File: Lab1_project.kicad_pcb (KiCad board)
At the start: 2 copper layers, 80 x 80 mm, 11 parts, among them J1 PROG, J2 POWER IN, U1 STM32F407IGTx, U2 AMS1117-3.3, Y1 8 MHz

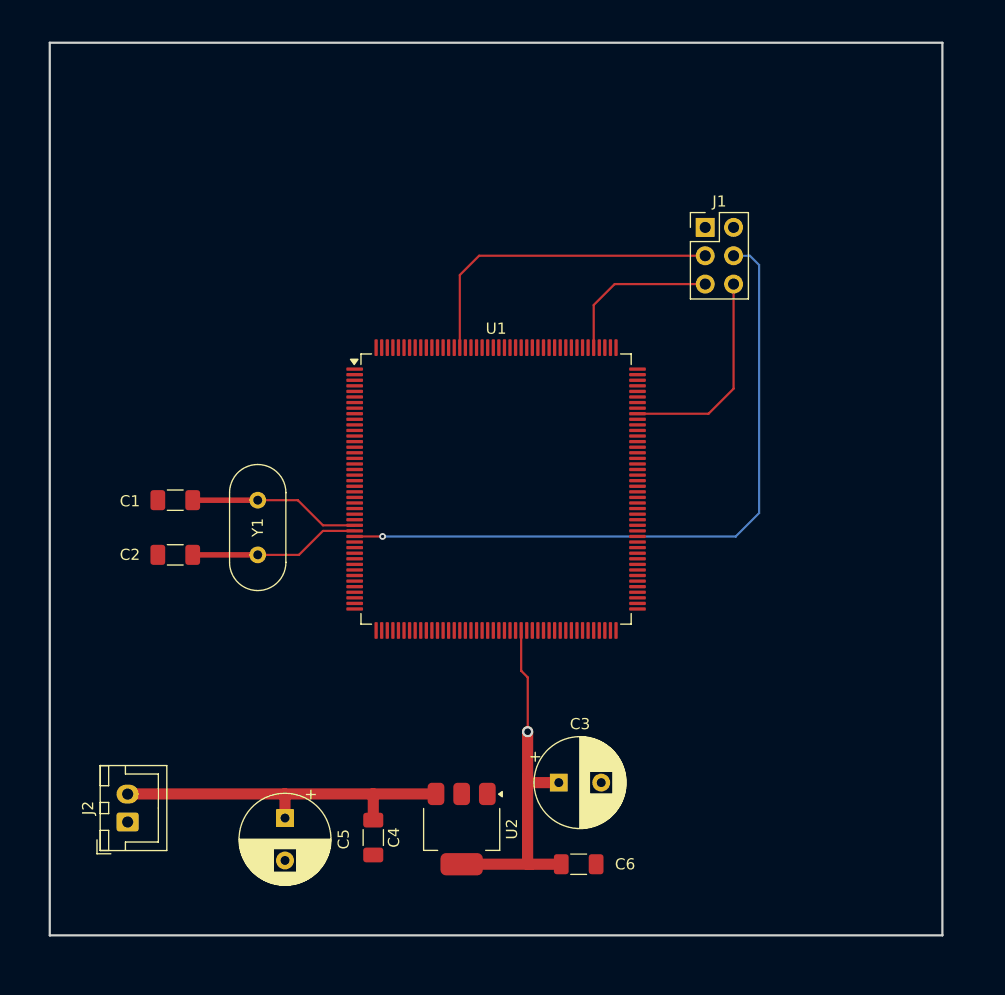
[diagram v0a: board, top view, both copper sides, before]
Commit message: fix: GND area, silkscreen
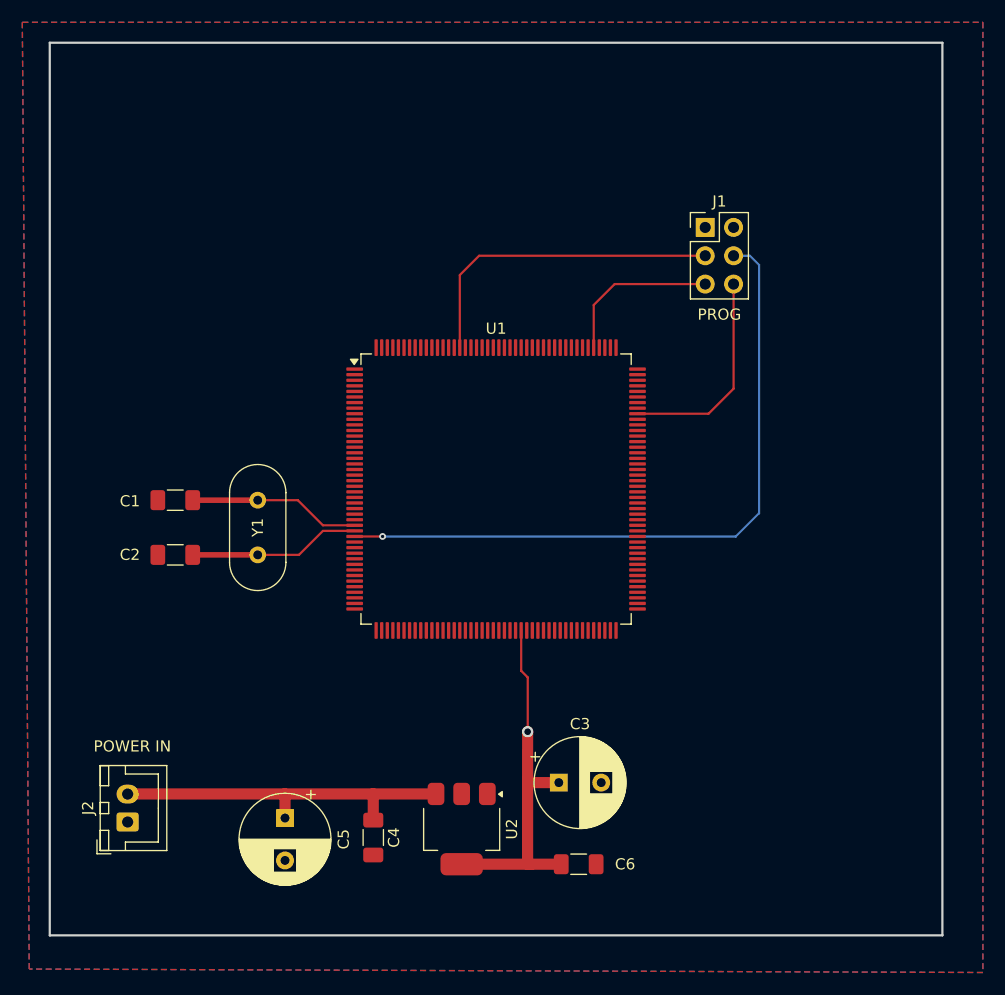
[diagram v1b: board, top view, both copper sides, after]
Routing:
- added copper zone on B.Cu, net GND
- added copper zone on F.Cu, net GND
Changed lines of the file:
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@@
 		(tags "connector JST XH vertical")
 		(property "Reference" "J2"
-			(at 1.25 -3.55 270)
+			(at 1.25 -3.55 -90)
 			(layer "F.SilkS")
 			(effects
@@
 		)
 		(property "Value" "POWER IN"
-			(at 1.25 4.6 270)
-			(layer "F.Fab")
+			(at 6.78 0.42 0)
+			(layer "F.SilkS")
 			(effects
 				(font
@@
 		)
 		(fp_text user "${REFERENCE}"
-			(at 1.25 2.7 270)
+			(at 1.25 2.7 -90)
 			(layer "F.Fab")
 			(effects
@@
 		)
 		(property "Value" "PROG"
-			(at 1.27 7.41 0)
-			(layer "F.Fab")
+			(at 1.27 7.8092 0)
+			(layer "F.SilkS")
 			(effects
 				(font
@@
 		(tags "capacitor handsolder")
 		(property "Reference" "C6"
-			(at 4.16 0 360)
+			(at 4.16 0 0)
 			(layer "F.SilkS")
 			(effects
@@
 		)
 		(property "Value" "0.1 uF"
-			(at 0 1.85 360)
+			(at 0 1.85 0)
 			(layer "F.Fab")
 			(hide yes)
@@
 		)
 		(fp_text user "${REFERENCE}"
-			(at 0 0 360)
+			(at 0 0 0)
 			(layer "F.Fab")
 			(effects
@@
 		(tags "CP Radial series Radial pin pitch 3.80mm  diameter 8mm Electrolytic Capacitor")
 		(property "Reference" "C3"
-			(at 1.9 -5.25 360)
+			(at 1.9 -5.25 0)
 			(layer "F.SilkS")
 			(effects
@@
 		)
 		(property "Value" "470 uF"
-			(at 1.9 5.25 360)
+			(at 1.9 5.25 0)
 			(layer "F.Fab")
 			(hide yes)
@@
 		)
 		(fp_text user "${REFERENCE}"
-			(at 1.9 0 360)
+			(at 1.9 0 0)
 			(layer "F.Fab")
 			(effects
@@
 		(net 9)
 	)
+	(zone
+		(net 1)
+		(net_name "GND")
+		(layers "F&B.Cu")
+		(hatch edge 0.5)
+		(connect_pads
+			(clearance 0.5)
+		)
+		(min_thickness 0.25)
+		(filled_areas_thickness no)
+		(fill yes
+			(thermal_gap 0.5)
+			(thermal_bridge_width 0.5)
+		)
+		(polygon
+			(pts
+				(xy 105.71 49.17) (xy 191.8 49.17) (xy 191.8 134.33) (xy 106.33 134.02)
+			)
+		)
+	)
 )
